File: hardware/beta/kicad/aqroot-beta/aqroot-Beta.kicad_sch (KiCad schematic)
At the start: 0 parts

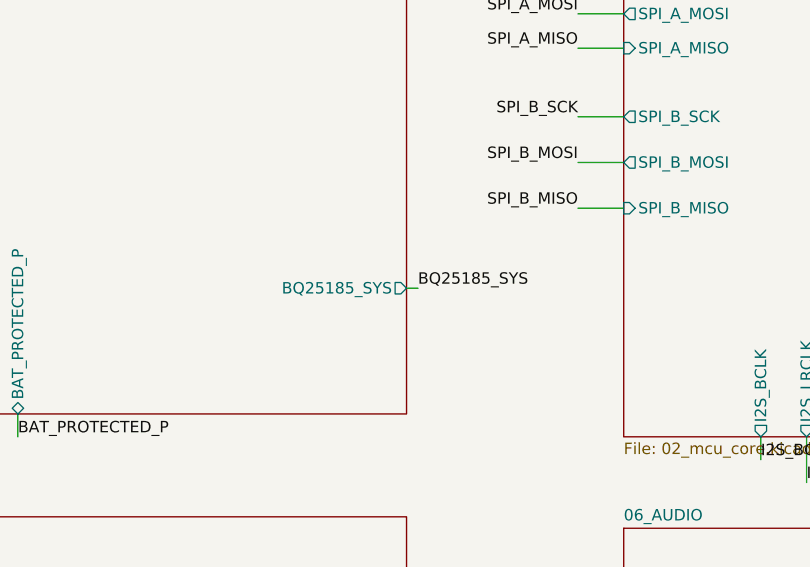
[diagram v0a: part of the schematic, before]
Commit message: AQROOT Beta: make BQ25185 SYS rail sheet-local
BQ25185_SYS was exported from 01_POWER_TREE through a root sheet pin to a
1.27 mm stub wire and a root label that nothing else consumed, so the root
label raised label_dangling.

Investigation classified the rail as genuinely sheet-internal: no other
sheet declares a BQ25185_SYS sheet pin, and all 12 electrical members
(C24.1 C26.2 C27.1 C28.1 C33.1 L2.1 SW9.1 U11.1 U12.1 U12.10 U12.11 U13.3)
sit inside 01_POWER_TREE. Every documentation reference - 01 Hardware Core,
05 Decisions Log, 07 Build TODO, 11 Pin Map and the KiCad README - describes
it as the internal rail feeding TPS63020 and TPS61023.

The hierarchy is therefore removed at BOTH levels, so no orphaned sheet pin
is left behind:
  01_power_tree: hierarchical label at (73.66, 97.79) -> plain local label
  root: sheet pin BQ25185_SYS removed (df685130)
  root: stub wire (105.41,88.9)-(106.68,88.9) removed (7c684050)
  root: label BQ25185_SYS at (106.68,88.9) removed (ed35ecf6)

Internal connectivity is untouched - the rail is still named by the 10
remaining local labels plus the converted one.

Verified with kicad-cli: all 12 members identical before and after. The
only netlist change is the expected scope demotion /BQ25185_SYS ->
/01_POWER_TREE/BQ25185_SYS on exactly those 12 pins; no other pin changed
net. label_dangling clears, zero new violations. Real ERC 7 -> 6.
Exclusions still 20, severities unchanged.

Co-Authored-By: Claude Opus 5 <noreply@anthropic.com>
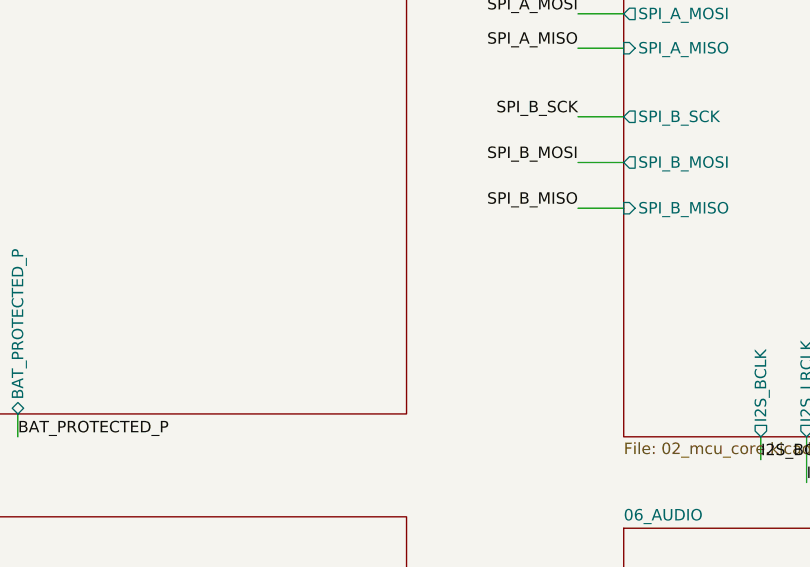
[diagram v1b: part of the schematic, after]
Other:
- sheet 01_POWER_TREE ports: added none; removed BQ25185_SYS
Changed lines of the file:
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@@
-	(wire
-		(pts
-			(xy 105.41 88.9) (xy 106.68 88.9)
-		)
-		(stroke
-			(width 0)
-			(type default)
-		)
-	)
 	(wire
 		(pts
@@
 	(label "XGPIO6"
 		(at 135.89 233.68 0)
-		(effects
-			(font
-				(size 1.27 1.27)
-			)
-			(justify left bottom)
-		)
-	)
-	(label "BQ25185_SYS"
-		(at 106.68 88.9 0)
 		(effects
 			(font
@@
 			)
 		)
-		(pin "BQ25185_SYS" output
-			(at 105.41 88.9 0)
-			(effects
-				(font
-					(size 1.27 1.27)
-				)
-				(justify right)
-			)
-		)

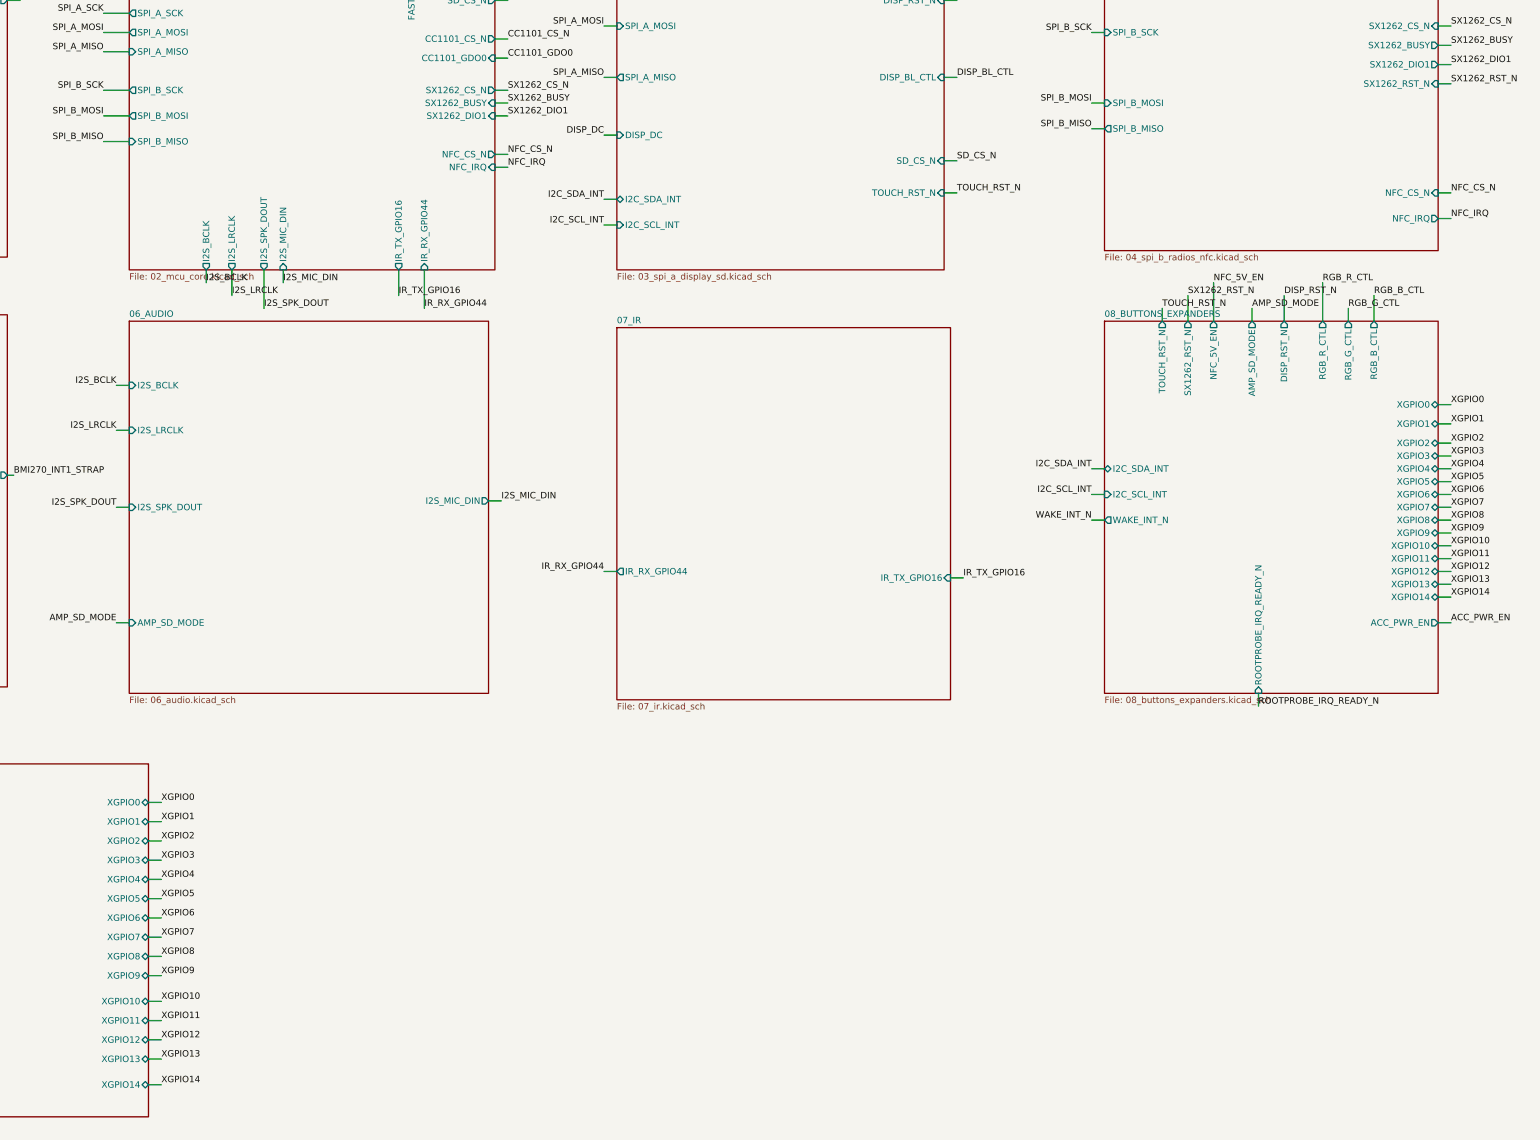
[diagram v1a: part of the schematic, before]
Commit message: AQROOT Beta: integrate E22 module and dedicate XGPIO14 to RX control
Atomic change across four files - root, sheet 04, sheet 08 and sheet 09 -
because the hierarchy reallocation and the module capture are electrically
coupled and neither is valid alone.

APPLIED TO U8, NOT U7. The schematic is authoritative: U8 is the SX1262 /
E22-900M22S at 915 MHz and U7 remains the CC1101 / E07-400M10S at 433 MHz. The
earlier blocker-register transposition is corrected and annotated in the log;
U7 is untouched and still a placeholder awaiting its own vendor audit.

U8 CAPTURE. The SX1262_MODULE_PLACEHOLDER is replaced by the physical 22-pin
E22-900M22S symbol on AQROOT_Beta:Ebyte_E22-900M22S. All 22 pads resolve, none
unconnected: the ten physical grounds - pins 1 to 5, 10, 11, 12, 20 and 22 - all
land on GND individually rather than being collapsed, pin 9 VCC is on +3V3, and
pins 13 to 19 carry SX1262_DIO1, SX1262_BUSY, SX1262_RST_N, SPI_B_MISO,
SPI_B_MOSI, SPI_B_SCK and SX1262_CS_N respectively. The seven existing
hierarchical labels were relocated onto the new pin stubs rather than
duplicated.

RF SWITCH. DIO2 on pin 8 is strapped locally to TXEN on pin 7, and the netlist
confirms DIO2_TXEN contains exactly those two nodes and nothing else, so no MCU
or expander pin is consumed for transmit control. Firmware must enable
SetDIO2AsRfSwitchCtrl or TXEN never asserts. Receive control comes from
SX1262_RXEN, which contains exactly U3 pin 19, U8 pin 6 and the new R74
pulldown.

XGPIO14 RETIRED. U3 pin 19 is reallocated from XGPIO14 to SX1262_RXEN across the
whole hierarchy - the sheet 08 hierarchical label, the sheet 08 sheet pin in the
root, and a new sheet 04 sheet pin plus root label. On sheet 09 the community
path is removed: R65 and its wires are deleted, the XGPIO14 hierarchical label
is gone, and both XGPIO14_HDR labels become RESERVED_NC, so J5 pin 19 no longer
advertises a GPIO. D6's now-spare ESD channel carries an explicit no_connect.
XGPIO0 to XGPIO13 are untouched and a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
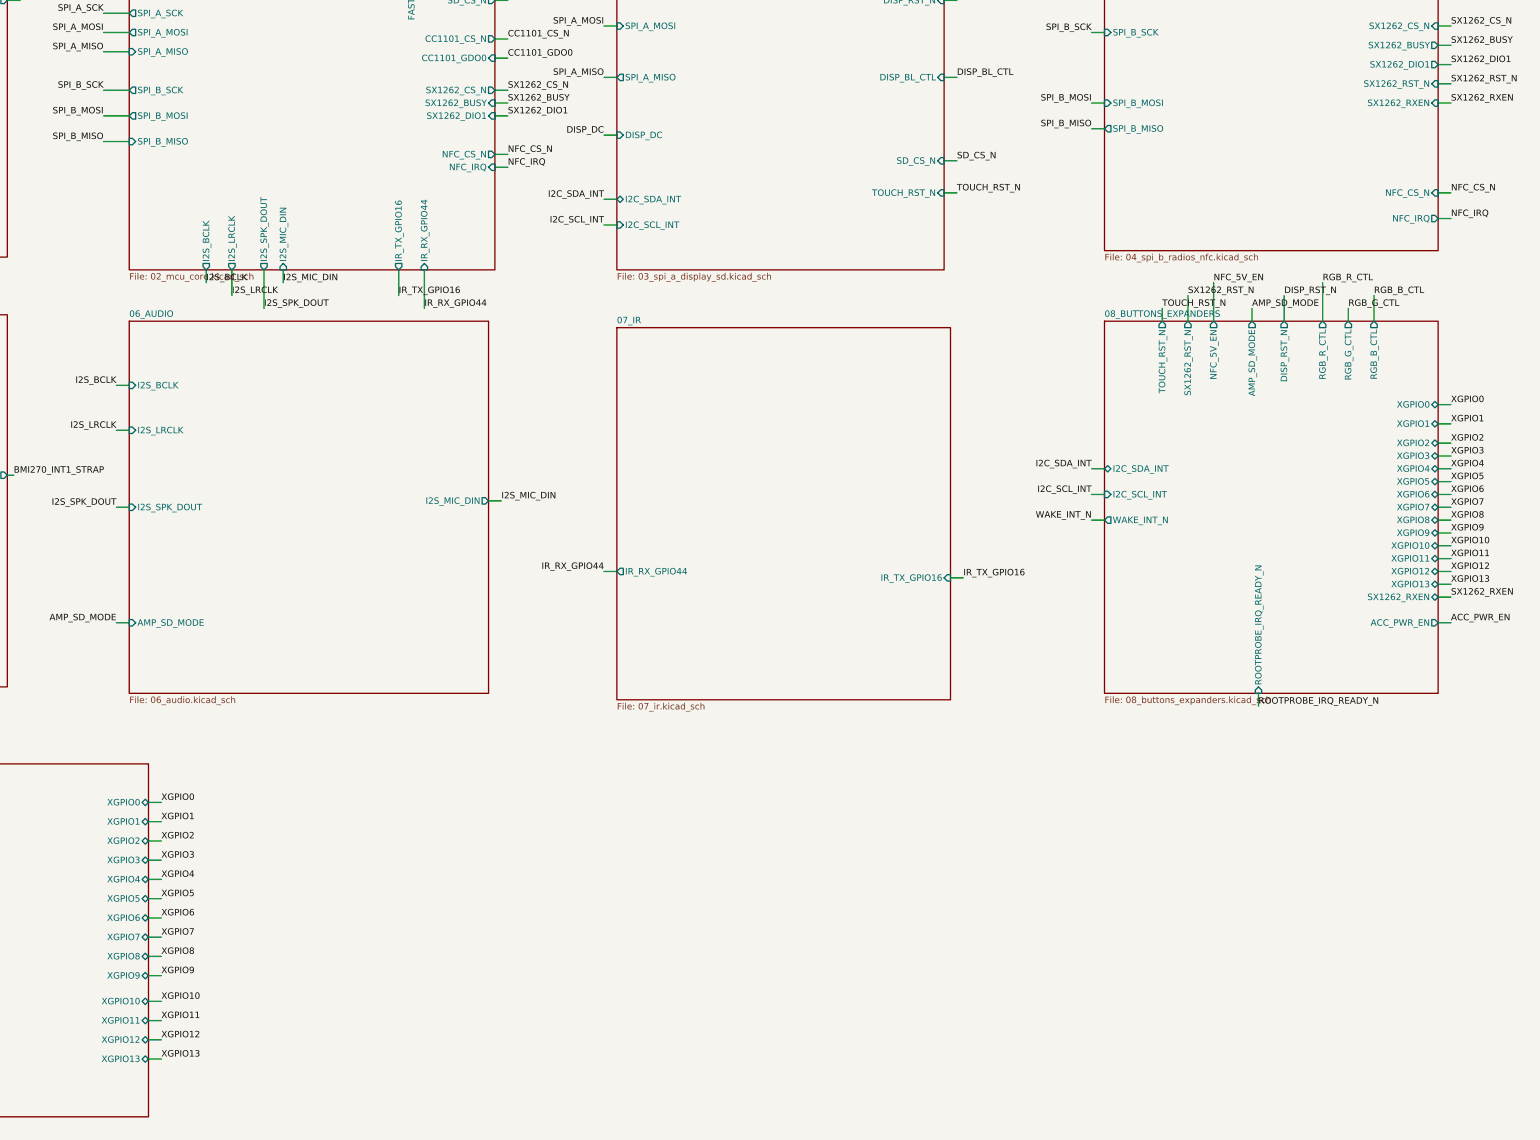
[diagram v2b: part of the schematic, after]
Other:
- sheet 04_SPI_B_RADIOS_NFC ports: added SX1262_RXEN; removed none
- sheet 08_BUTTONS_EXPANDERS ports: added SX1262_RXEN; removed XGPIO14
- sheet 09_COMMUNITY_HEADER ports: added none; removed XGPIO14
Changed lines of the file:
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@@
 	(wire
 		(pts
-			(xy 133.35 266.7) (xy 135.89 266.7)
-		)
-		(stroke
-			(width 0)
-			(type default)
-		)
-	)
-	(wire
-		(pts
 			(xy 388.62 64.77) (xy 391.16 64.77)
 		)
@@
 		)
 	)
-	(label "XGPIO14"
+	(label "SX1262_RXEN"
 		(at 391.16 170.18 0)
 		(effects
@@
 		)
 	)
-	(label "XGPIO14"
-		(at 135.89 266.7 0)
-		(effects
-			(font
-				(size 1.27 1.27)
-			)
-			(justify left bottom)
-		)
-	)
 	(label "XGPIO1"
 		(at 391.16 135.89 0)
@@
 			)
 		)
+		(pin "SX1262_RXEN" input
+			(at 388.62 72.39 0)
+			(effects
+				(font
+					(size 1.27 1.27)
+				)
+				(justify left)
+			)
+		)
 		(instances
 			(project "aqroot-Beta"
@@
 			)
 		)
-		(pin "XGPIO14" bidirectional
+		(pin "SX1262_RXEN" bidirectional
 			(at 388.62 170.18 0)
 			(effects
@@
 			)
 		)
-		(pin "XGPIO14" bidirectional
-			(at 133.35 266.7 0)
-			(effects
-				(font
-					(size 1.27 1.27)
-				)
-				(justify right)
-			)
-		)
 		(instances
 			(project "aqroot-Beta"
@@
 	)
 	(embedded_fonts no)
+	(wire
+		(pts
+			(xy 388.62 72.39) (xy 391.16 72.39)
+		)
+		(stroke
+			(width 0)
+			(type default)
+		)
+	)
+	(label "SX1262_RXEN"
+		(at 391.16 72.39 0)
+		(effects
+			(font
+				(size 1.27 1.27)
+			)
+			(justify left bottom)
+		)
+	)
 )

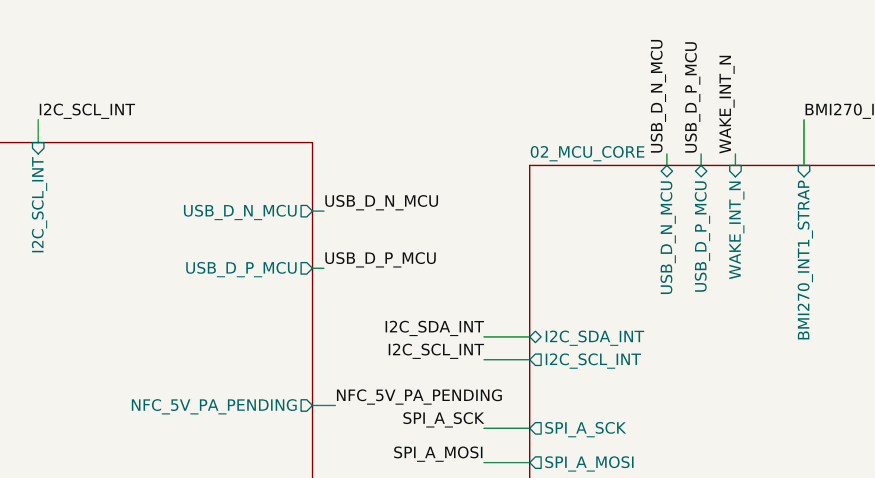
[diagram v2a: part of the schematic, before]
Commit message: AQROOT Beta: close final routing blockers
Closes the two BLOCKS_ROUTING items left by the pre-routing rule pass.
No traces drawn, no component moved, aqroot-Beta.kicad_dru untouched.

1. BQ25185 charge current locked at 300 mA.

R37 2k 1% -> 1k 1% on the ISET pin. ICHG = KISET/RISET = 300/1000 =
300 mA typ, 285/300/315 mA from the KISET spread and 270-330 mA at
TI's +/-10% ICHG_ACC spec. 0.15 C on the 2000 mAh Beta pack. IPRECHG
rises to 60 mA and ITERM to 30 mA. 1 kohm is TI's own figure in
SLUSF65A section 8.2.2.2, is far above RISET_SHORT (264 ohm), and
300 mA is far below the 1 A device maximum, so nothing is clipped.

R36 = 18 kohm is untouched: the input current limit stays ILIM500
(450/475/498 mA) and VBATREG stays 4.2 V. Both the schematic symbol and
the PCB footprint Value field were updated together, so parity picks up
no new field mismatch.

No power netclass width target changes. VBUS_CHG is set by ILIM, which
did not move; BAT_MAIN is sized by 1.5 A discharge and 3.125 A OCP;
SYS_MAIN is sized by the ~750 mA system load. IPC-2221B needs 0.057 mm
for 300 mA on 1 oz outer copper at dT=10 K, an order of magnitude below
every existing floor, so nothing was widened.

The real consequence is thermal and lands on U11. As a linear charger
with a power path, worst-case dissipation rises from ~0.46 W to ~0.69 W
(0.238 W on IN->SYS at 475 mA plus 0.450 W on the BATFET at 300 mA into
a depleted 3.0 V pack) in a 2.2 x 2.0 mm WSON-10. TREG folds charge
current back rather than failing, so this is a charge-time risk, but
U11's exposed-pad thermal vias are now required rather than optional
and the plan is revised from 1 to 2 THERMAL-class vias. Implementation
stays deferred to the routing/thermal pass.

Added BOM VERIFY: the cell/pack must permit >=300 mA charge, including
the pack protection circuit's own rating. Blocks BOM lock, not routing.

2. USB differential net names normalised to a _P/_N suffix.

  USB_D_P_CONN -> USB_D_CONN_P    USB_D_N_CONN -> USB_D_CONN_N
  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
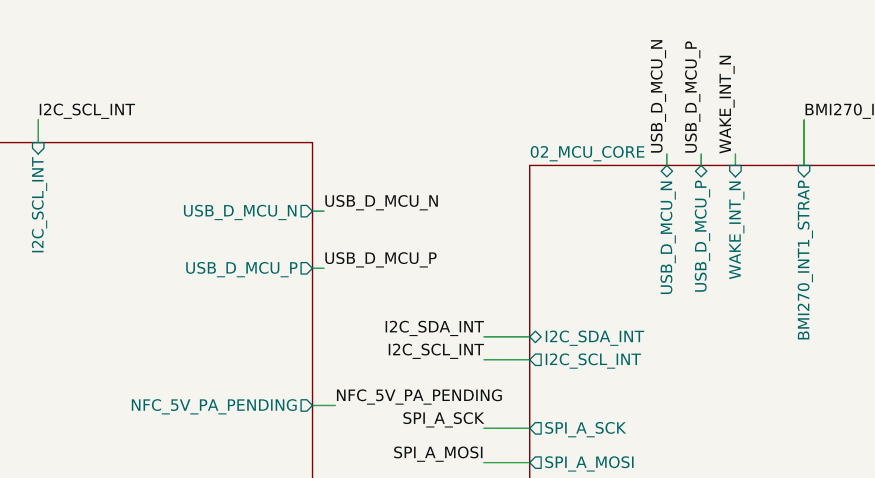
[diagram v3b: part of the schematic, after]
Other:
- sheet 01_POWER_TREE ports: added USB_D_MCU_N, USB_D_MCU_P; removed USB_D_N_MCU, USB_D_P_MCU
- sheet 02_MCU_CORE ports: added USB_D_MCU_N, USB_D_MCU_P; removed USB_D_N_MCU, USB_D_P_MCU
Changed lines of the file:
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@@
 		)
 	)
-	(label "USB_D_N_MCU"
+	(label "USB_D_MCU_N"
 		(at 106.68 30.48 0)
 		(effects
@@
 		)
 	)
-	(label "USB_D_P_MCU"
+	(label "USB_D_MCU_P"
 		(at 148.59 24.13 90)
 		(effects
@@
 		)
 	)
-	(label "USB_D_P_MCU"
+	(label "USB_D_MCU_P"
 		(at 106.68 36.83 0)
 		(effects
@@
 		)
 	)
-	(label "USB_D_N_MCU"
+	(label "USB_D_MCU_N"
 		(at 144.78 24.13 90)
 		(effects
@@
 			)
 		)
-		(pin "USB_D_N_MCU" output
+		(pin "USB_D_MCU_N" output
 			(at 105.41 30.48 0)
 			(effects
@@
 			)
 		)
-		(pin "USB_D_P_MCU" output
+		(pin "USB_D_MCU_P" output
 			(at 105.41 36.83 0)
 			(effects
@@
 			)
 		)
-		(pin "USB_D_N_MCU" bidirectional
+		(pin "USB_D_MCU_N" bidirectional
 			(at 144.78 25.4 90)
 			(effects
@@
 			)
 		)
-		(pin "USB_D_P_MCU" bidirectional
+		(pin "USB_D_MCU_P" bidirectional
 			(at 148.59 25.4 90)
 			(effects
